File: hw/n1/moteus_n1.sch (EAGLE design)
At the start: 192 parts, among them J1 XT30XT30PW_MALE, J2 XT30XT30PW_MALE, J3 SM06B-GHS-TB(LF)(SN), M1 MOUNT, M2 MOUNT, M3 MOUNT, M4 MOUNT, Q1 TPH1R204PL_VIAS, Q2 TPH1R204PLSOP_ADVANCE_8, Q3 TPH1R204PL_VIAS, Q4 TPH1R204PLSOP_ADVANCE_8, Q5 TPH1R204PL_VIAS, Q6 TPH1R204PLSOP_ADVANCE_8, U1 MAX15062AATA+T, U2 ADP5301ACBZ-4-R7, U3 STM32G474CEU6, U4 TCAN1042HGV, U5 AS5147, U7 DRV8353S, U8 SN65HVD35DR

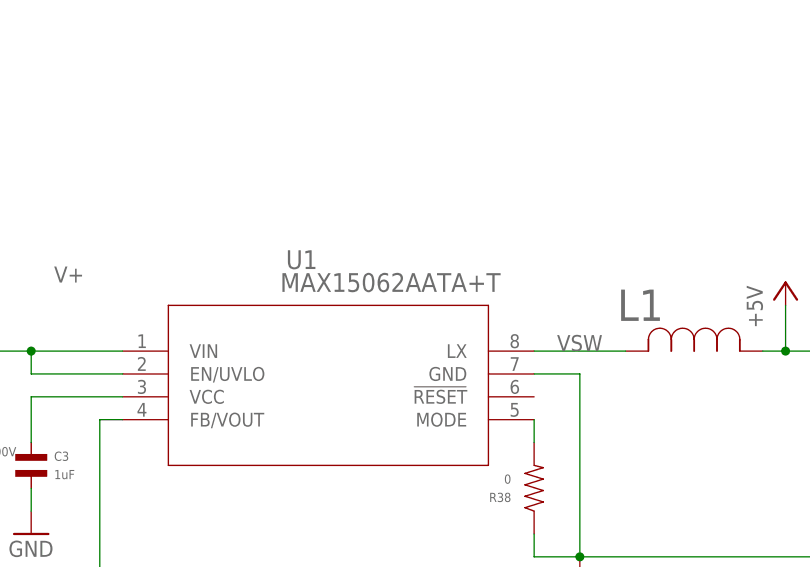
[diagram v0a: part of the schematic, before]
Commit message: Update the moteus-n1 5V regulator "value" to be MAX15062BATA+T
The MPN attribute was always correct and is canonical, but this makes
confusion less likely.
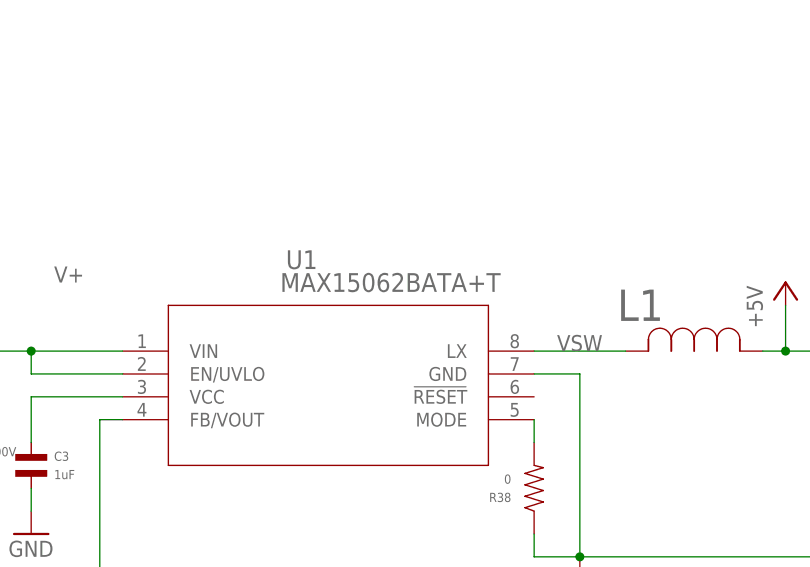
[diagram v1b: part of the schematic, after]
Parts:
- U1: value MAX15062AATA+T -> MAX15062BATA+T
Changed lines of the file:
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@@
 <attribute name="POPULATE" value="1"/>
 </part>
-<part name="U1" library="power_dist" deviceset="MAX15062AATA+T" device="">
+<part name="U1" library="power_dist" deviceset="MAX15062AATA+T" device="" value="MAX15062BATA+T">
 <attribute name="MANUFACTURER_PART_NUMBER" value="MAX15062BATA+T"/>
 <attribute name="MF" value="Maxim"/>
